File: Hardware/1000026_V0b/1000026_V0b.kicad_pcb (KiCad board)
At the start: 4 copper layers, 100 x 70 mm, 29 parts, among them J1 533750410, J2 4390, J3 532580229, J5 532580229, J9 0525591853, SW1 TL3305CF260QG, U1 BD450M5FP-CE2, U2 MAX7480ESA+

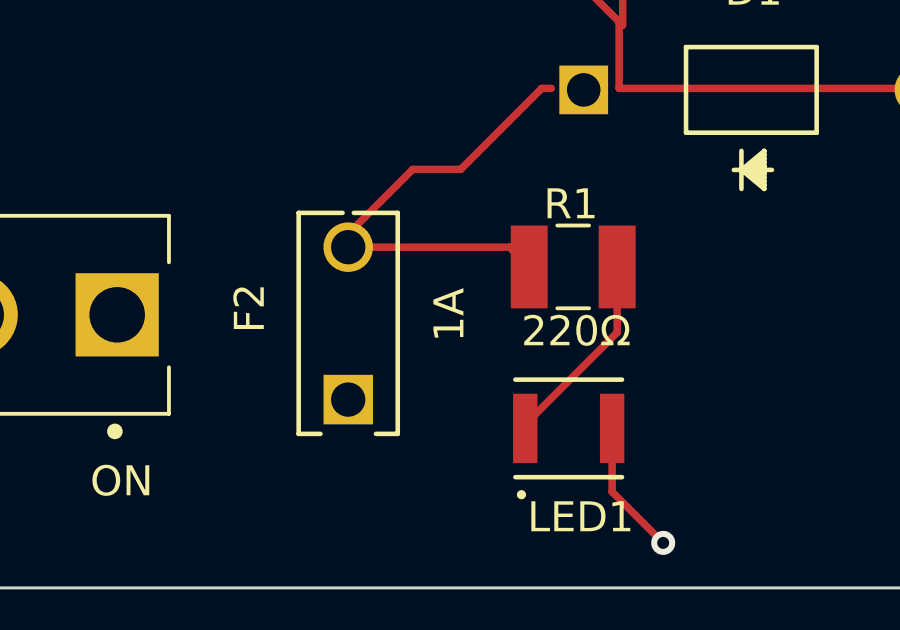
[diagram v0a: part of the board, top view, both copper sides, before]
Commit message: Updating KiCad library
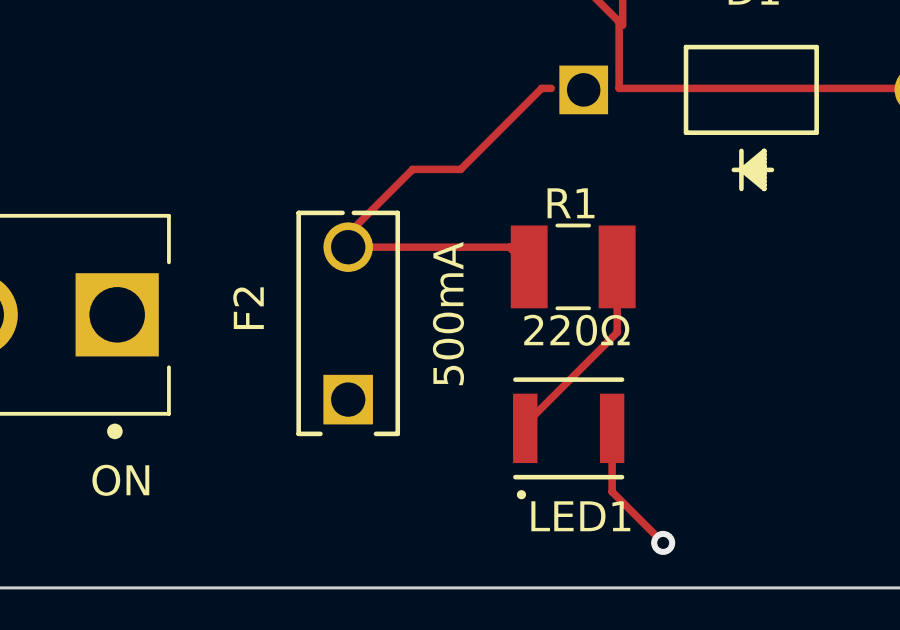
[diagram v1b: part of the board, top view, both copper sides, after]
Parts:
- F2: value FUSE_1A -> FUSE_500mA
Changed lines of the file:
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@@
 			)
 		)
-		(property "Value" "FUSE_1A"
-			(at -1.127374 2.85 90)
+		(property "Value" "FUSE_500mA"
+			(at -3 2.5 90)
 			(layer "F.SilkS")
 			(hide yes)
@@
 			)
 		)
-		(property "Footprint" ""
+		(property "Footprint" "RobotFtpLib:RKEF050HF"
 			(at 0 0 90)
 			(layer "F.Fab")
@@
 			(layer "F.Fab")
 		)
-		(fp_text user "1A"
+		(fp_text user "500mA"
 			(at 2.8194 3.3782 90)
 			(unlocked yes)

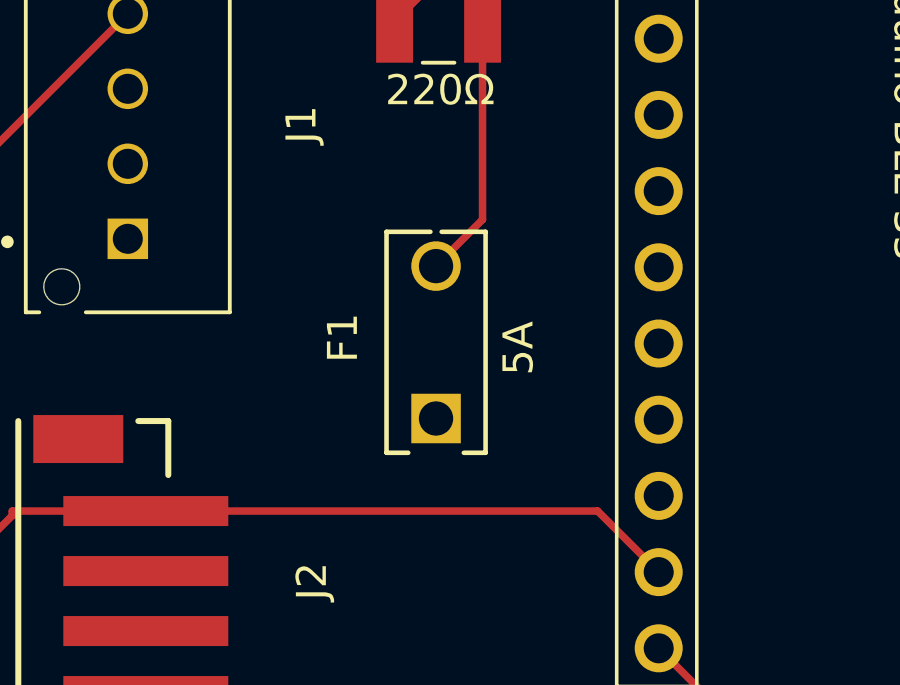
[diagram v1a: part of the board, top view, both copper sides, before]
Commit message: Updating KiCad library
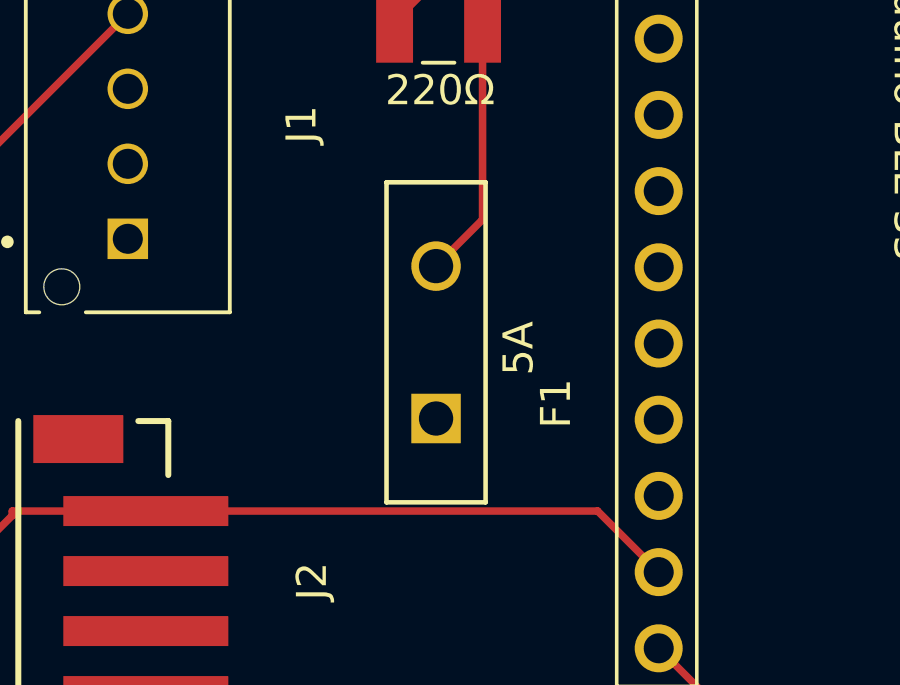
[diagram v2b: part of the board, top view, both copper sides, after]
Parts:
- F1: footprint RobotFtpLib:RGEF300HF -> RobotFtpLib:RGEF500HF
- S1: value 500SSP1S2M2QEA -> Slider_switch_500SSP1S2M2QEA
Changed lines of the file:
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@@
 			)
 		)
-		(property "Footprint" ""
+		(property "Footprint" "RobotFtpLib:0532580229"
 			(at 0 0 -90)
 			(layer "F.Fab")
@@
 			)
 		)
+		(fp_text user "532580229"
+			(at -1.749991 -12.835001 -90)
+			(unlocked yes)
+			(layer "F.Fab")
+			(hide yes)
+			(effects
+				(font
+					(size 1 1)
+					(thickness 0.2)
+				)
+			)
+		)
 		(fp_text user "${REFERENCE}"
 			(at -1.749991 -8.89 -90)
-			(unlocked yes)
-			(layer "F.Fab")
-			(hide yes)
-			(effects
-				(font
-					(size 1 1)
-					(thickness 0.2)
-				)
-			)
-		)
-		(fp_text user "532580229"
-			(at -1.749991 -12.835001 -90)
 			(unlocked yes)
 			(layer "F.Fab")
@@
 		)
 	)
-	(footprint "RobotFtpLib:RGEF300HF"
+	(footprint "RobotFtpLib:RGEF500HF"
 		(layer "F.Cu")
 		(at 116.4898 90.0532 90)
+		(tags "RGEF500 ")
 		(property "Reference" "F1"
-			(at 2.69 -3.1 90)
-			(layer "F.SilkS")
-			(effects
-				(font
-					(size 1 1)
-					(thickness 0.2)
+			(at 0.5 4 90)
+			(unlocked yes)
+			(layer "F.SilkS")
+			(effects
+				(font
+					(size 1 1)
+					(thickness 0.15)
 				)
 			)
 		)
 		(property "Value" "FUSE_5A"
-			(at 1.9812 4.1402 90)
-			(layer "F.SilkS")
-			(hide yes)
-			(effects
-				(font
-					(size 1 1)
-					(thickness 0.2)
-				)
-			)
-		)
-		(property "Footprint" ""
+			(at 3 -5 90)
+			(unlocked yes)
+			(layer "F.Fab")
+			(effects
+				(font
+					(size 1 1)
+					(thickness 0.15)
+				)
+			)
+		)
+		(property "Footprint" "RobotFtpLib:RGEF500HF"
 			(at 0 0 90)
 			(layer "F.Fab")
@@
 		(attr through_hole)
 		(fp_line
-			(start 6.223 -1.651)
-			(end -1.143 -1.651)
-			(stroke
-				(width 0.1524)
-				(type solid)
-			)
-			(layer "F.SilkS")
-		)
-		(fp_line
-			(start -1.143 -1.651)
-			(end -1.143 -0.925047)
-			(stroke
-				(width 0.1524)
-				(type solid)
-			)
-			(layer "F.SilkS")
-		)
-		(fp_line
-			(start 6.223 -0.187272)
-			(end 6.223 -1.651)
-			(stroke
-				(width 0.1524)
-				(type solid)
-			)
-			(layer "F.SilkS")
-		)
-		(fp_line
-			(start -1.143 0.925047)
-			(end -1.143 1.651)
-			(stroke
-				(width 0.1524)
-				(type solid)
-			)
-			(layer "F.SilkS")
-		)
-		(fp_line
-			(start 6.223 1.651)
-			(end 6.223 0.187272)
-			(stroke
-				(width 0.1524)
-				(type solid)
-			)
-			(layer "F.SilkS")
-		)
-		(fp_line
-			(start -1.143 1.651)
-			(end 6.223 1.651)
-			(stroke
-				(width 0.1524)
-				(type solid)
-			)
-			(layer "F.SilkS")
-		)
-		(fp_line
-			(start 6.35 -1.778)
-			(end 6.35 1.778)
-			(stroke
-				(width 0.1524)
-				(type solid)
-			)
-			(layer "F.CrtYd")
-		)
-		(fp_line
-			(start -1.27 -1.778)
-			(end 6.35 -1.778)
-			(stroke
-				(width 0.1524)
-				(type solid)
-			)
-			(layer "F.CrtYd")
-		)
-		(fp_line
-			(start 6.35 1.778)
-			(end -1.27 1.778)
-			(stroke
-				(width 0.1524)
-				(type solid)
-			)
-			(layer "F.CrtYd")
-		)
-		(fp_line
-			(start -1.27 1.778)
-			(end -1.27 -1.778)
-			(stroke
-				(width 0.1524)
-				(type solid)
-			)
-			(layer "F.CrtYd")
-		)
-		(fp_line
-			(start 6.096 -1.524)
-			(end -1.016 -1.524)
-			(stroke
-				(width 0.1524)
-				(type solid)
-			)
-			(layer "F.Fab")
-		)
-		(fp_line
-			(start -1.016 -1.524)
-			(end -1.016 1.524)
-			(stroke
-				(width 0.1524)
-				(type solid)
-			)
-			(layer "F.Fab")
-		)
-		(fp_line
-			(start -1.016 -0.5334)
-			(end -0.0254 -1.524)
-			(stroke
-				(width 0.1524)
-				(type solid)
-			)
-			(layer "F.Fab")
-		)
-		(fp_line
-			(start 6.096 1.524)
-			(end 6.096 -1.524)
-			(stroke
-				(width 0.1524)
-				(type solid)
-			)
-			(layer "F.Fab")
-		)
-		(fp_line
-			(start -1.016 1.524)
-			(end 6.096 1.524)
-			(stroke
-				(width 0.1524)
+			(start 7.874 -1.651)
+			(end -2.794 -1.651)
+			(stroke
+				(width 0.1524)
+				(type solid)
+			)
+			(layer "F.SilkS")
+		)
+		(fp_line
+			(start -2.794 -1.651)
+			(end -2.794 1.651)
+			(stroke
+				(width 0.1524)
+				(type solid)
+			)
+			(layer "F.SilkS")
+		)
+		(fp_line
+			(start 7.874 1.651)
+			(end 7.874 -1.651)
+			(stroke
+				(width 0.1524)
+				(type solid)
+			)
+			(layer "F.SilkS")
+		)
+		(fp_line
+			(start -2.794 1.651)
+			(end 7.874 1.651)
+			(stroke
+				(width 0.1524)
+				(type solid)
+			)
+			(layer "F.SilkS")
+		)
+		(fp_line
+			(start 8.001 -1.778)
+			(end 8.001 1.778)
+			(stroke
+				(width 0.1524)
+				(type solid)
+			)
+			(layer "F.CrtYd")
+		)
+		(fp_line
+			(start -2.921 -1.778)
+			(end 8.001 -1.778)
+			(stroke
+				(width 0.1524)
+				(type solid)
+			)
+			(layer "F.CrtYd")
+		)
+		(fp_line
+			(start 8.001 1.778)
+			(end -2.921 1.778)
+			(stroke
+				(width 0.1524)
+				(type solid)
+			)
+			(layer "F.CrtYd")
+		)
+		(fp_line
+			(start -2.921 1.778)
+			(end -2.921 -1.778)
+			(stroke
+				(width 0.1524)
+				(type solid)
+			)
+			(layer "F.CrtYd")
+		)
+		(fp_line
+			(start 7.747 -1.524)
+			(end -2.667 -1.524)
+			(stroke
+				(width 0.0254)
+				(type solid)
+			)
+			(layer "F.Fab")
+		)
+		(fp_line
+			(start -2.667 -1.524)
+			(end -2.667 1.524)
+			(stroke
+				(width 0.0254)
+				(type solid)
+			)
+			(layer "F.Fab")
+		)
+		(fp_line
+			(start -2.667 -0.5334)
+			(end -1.6764 -1.524)
+			(stroke
+				(width 0.0254)
+				(type solid)
+			)
+			(layer "F.Fab")
+		)
+		(fp_line
+			(start 7.747 1.524)
+			(end 7.747 -1.524)
+			(stroke
+				(width 0.0254)
+				(type solid)
+			)
+			(layer "F.Fab")
+		)
+		(fp_line
+			(start -2.667 1.524)
+			(end 7.747 1.524)
+			(stroke
+				(width 0.0254)
 				(type solid)
 			)
@@
 					(size 1 1)
 					(thickness 0.2)
+				)
+			)
+		)
+		(fp_text user "F"
+			(at 1 -3 90)
+			(unlocked yes)
+			(layer "F.Fab")
+			(effects
+				(font
+					(size 1 1)
+					(thickness 0.15)
 				)
 			)
@@
 			)
 		)
-		(property "Value" "500SSP1S2M2QEA"
+		(property "Value" "Slider_switch_500SSP1S2M2QEA"
 			(at 0 8.128 180)
 			(layer "F.Fab")
@@
 			)
 		)
-		(property "Footprint" ""
+		(property "Footprint" "RobotFtpLib:500SSP1S2M2QEA"
 			(at 0 0 180)
 			(layer "F.Fab")
